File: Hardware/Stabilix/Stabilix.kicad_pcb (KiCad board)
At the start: 2 copper layers, 68.6 x 53.3 mm, 28 parts, among them J1 NEMA17-M1, J2 NEMA17-M2, J3 KF35-2P Battery, J4 Power Switch, J5 Servo, J6 Expansion, U1 AMS1117-5.0, U2 AMS1117-5.0, U3 A4988_STEPPER_MOTOR_DRIVER_CA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, U4 A4988_STEPPER_MOTOR_DRIVER_CA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, U5 module_mpu6050, U6 ESP32-DEVKIT-V1

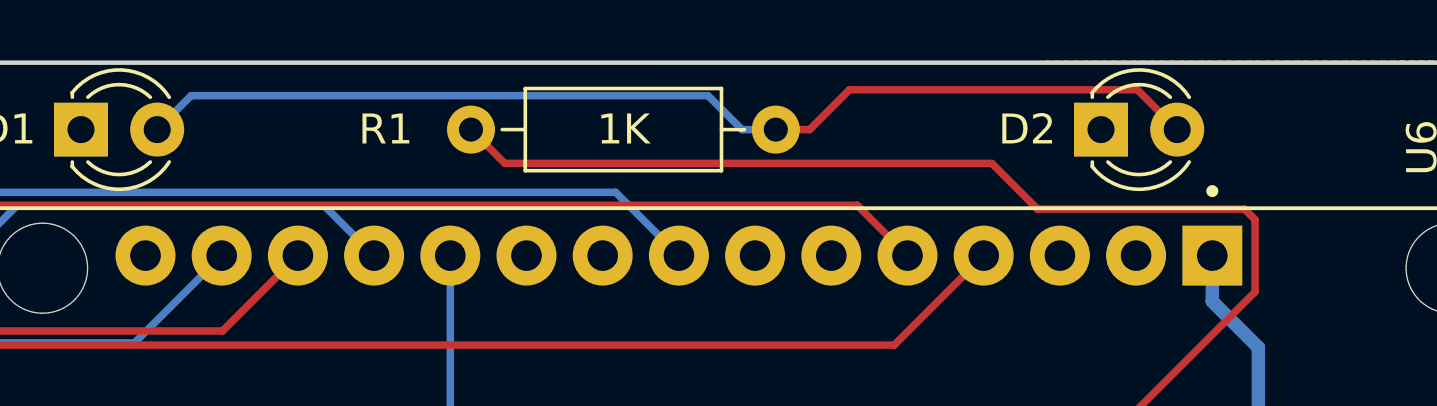
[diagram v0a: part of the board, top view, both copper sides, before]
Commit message: Footprint adjustments
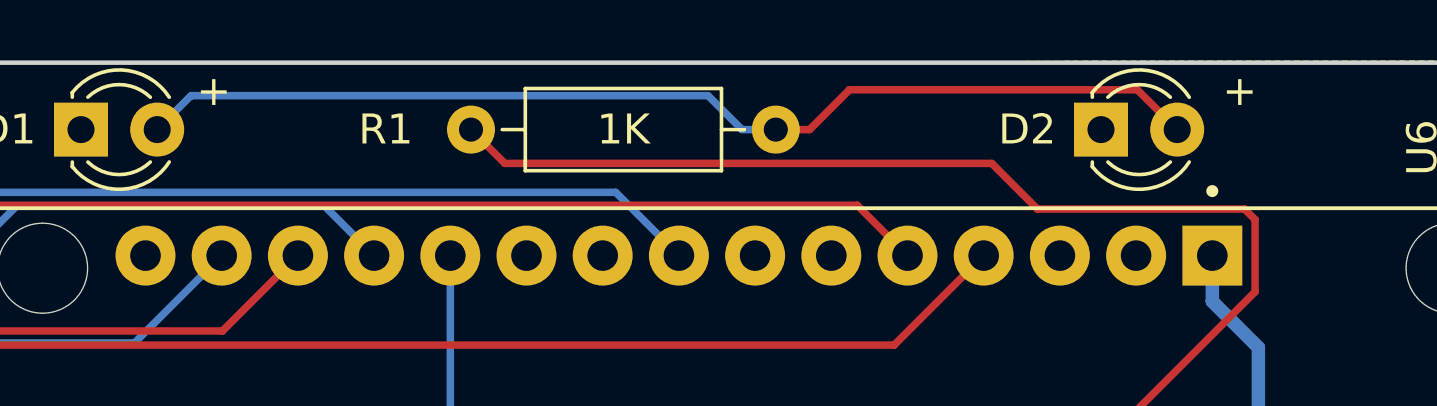
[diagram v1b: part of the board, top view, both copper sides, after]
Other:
- board text added: "+"
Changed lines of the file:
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@@
     (attr board_only exclude_from_pos_files exclude_from_bom)
     (fp_text reference "kibuzzard-6589FCE6" (at 0 -3.891492) (layer "F.SilkS") hide
-        (effects (font (size 0 0)))
+        (effects (font (size 0 0) (thickness 0.15)))
     )
     (fp_text value "G***" (at 0 3.891492) (layer "F.SilkS") hide
-        (effects (font (size 0 0)))
+        (effects (font (size 0 0) (thickness 0.15)))
     )
     (fp_poly
@@
     (pad "2" thru_hole circle (at 5.08 0 270) (size 3 3) (drill 1.52) (layers "*.Cu" "*.Mask")
       (net 42 "Net-(J3-Pin_2)") (pinfunction "Pin_2") (pintype "passive"))
-    (model "${KIPRJMOD}/libraries/TerminalBlock_bornier-2_P5.08mm.wrl"
-      (offset (xyz 2.54 0 0))
+    (model "${KICAD7_3DMODEL_DIR}/TerminalBlock_Phoenix.3dshapes/TerminalBlock_Phoenix_MKDS-1,5-2_1x02_P5.00mm_Horizontal.wrl"
+      (offset (xyz 0 0 0))
       (scale (xyz 1 1 1))
       (rotate (xyz 0 0 0))
@@
     (attr board_only exclude_from_pos_files exclude_from_bom)
     (fp_text reference "kibuzzard-6589FE5A" (at 0 -3.881173) (layer "F.SilkS") hide
-        (effects (font (size 0 0)))
+        (effects (font (size 0 0) (thickness 0.15)))
     )
     (fp_text value "G***" (at 0 3.881173) (layer "F.SilkS") hide
-        (effects (font (size 0 0)))
+        (effects (font (size 0 0) (thickness 0.15)))
     )
     (fp_poly
@@
     (attr board_only exclude_from_pos_files exclude_from_bom)
     (fp_text reference "kibuzzard-6589FE3E" (at 0 -3.87006) (layer "F.SilkS") hide
-        (effects (font (size 0 0)))
+        (effects (font (size 0 0) (thickness 0.15)))
     )
     (fp_text value "G***" (at 0 3.87006) (layer "F.SilkS") hide
-        (effects (font (size 0 0)))
+        (effects (font (size 0 0) (thickness 0.15)))
     )
     (fp_poly
@@
     (effects (font (size 0.8 0.8) (thickness 0.15)) (justify left bottom))
   )
+  (gr_text "+" (at 125 70.8) (layer "F.SilkS")
+    (effects (font (size 1 1) (thickness 0.15)) (justify left bottom mirror))
+  )
   (gr_text "D4" (at 109.1 78.2) (layer "F.SilkS")
     (effects (font (size 0.8 0.8) (thickness 0.15)) (justify left bottom))
   )
+  (gr_text "+" (at 159.2 70.8) (layer "F.SilkS")
+    (effects (font (size 1 1) (thickness 0.15)) (justify left bottom mirror))
+  )
   (gr_text "3V3" (at 103.8 78.2) (layer "F.SilkS")

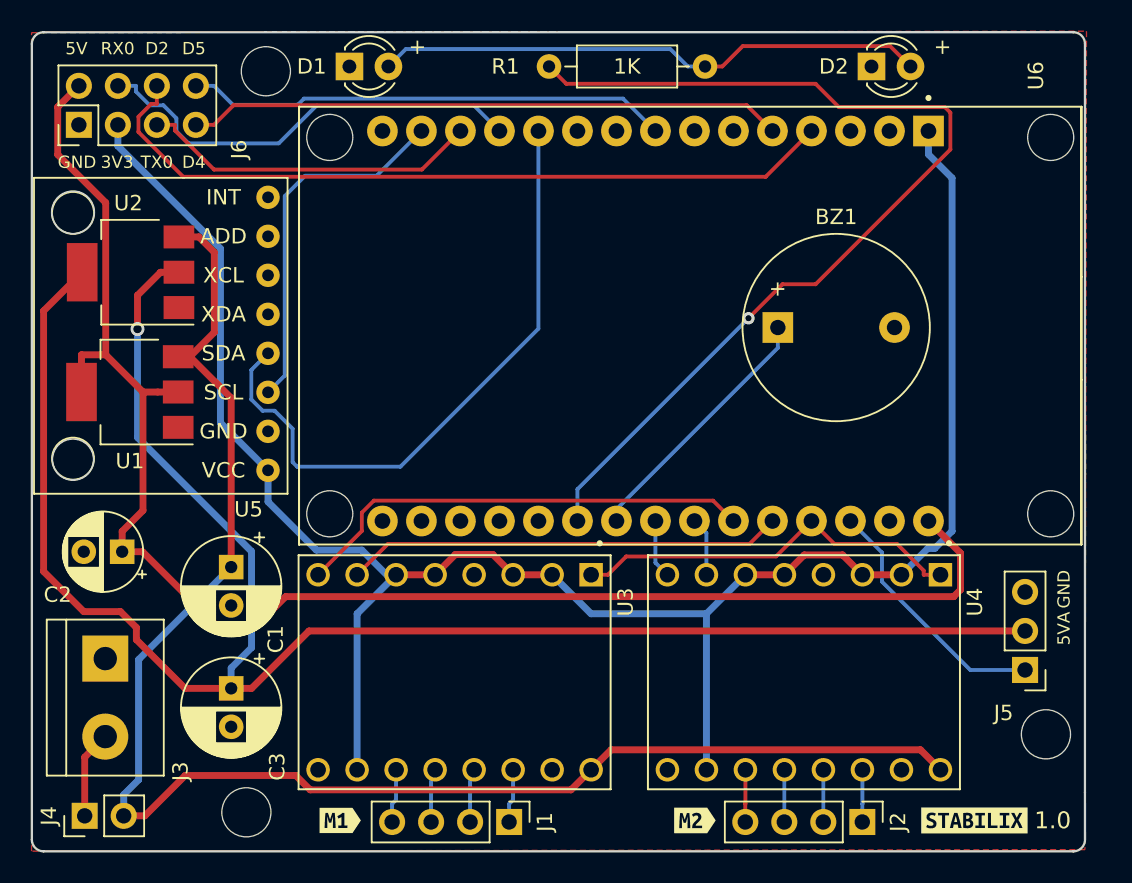
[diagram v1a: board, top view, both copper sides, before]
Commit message: fixes on the screw holes
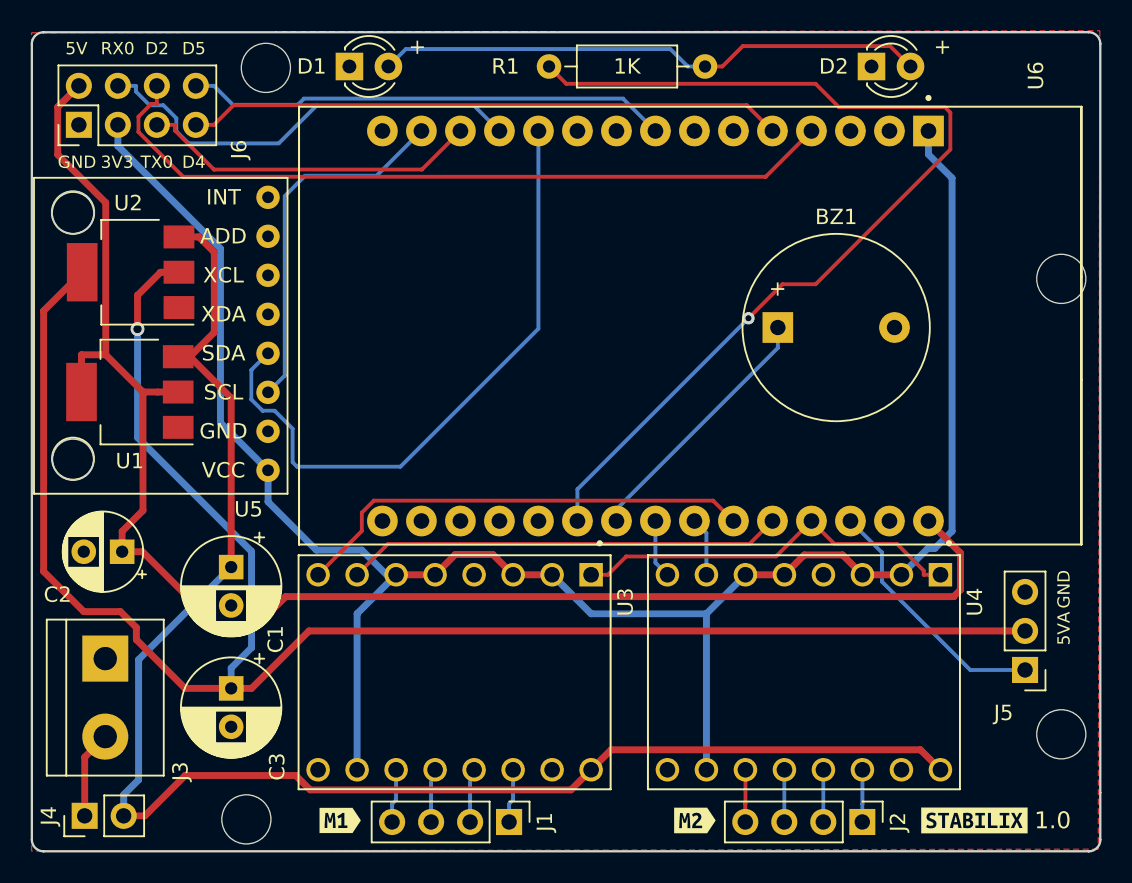
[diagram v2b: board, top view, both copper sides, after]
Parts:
- added MH4: MountingHole_3.2mm, Arduino_MountingHole:MountingHole_3.2mm, F.Cu at (166.4, 85.3)
- moved MH4 1.00 mm to (166.4, 115.0)
- moved MH2 0.23 mm to (113.3, 120.3)
- moved MH1 0.11 mm to (114.6, 71.7)
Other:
- board size 68.6 x 53.3 mm -> 69.6 x 53.3 mm
- board text added: "Stabilix Self-Balancing Robot Based on JJRobots open source B-Robot EVO project"
- board text added: "crisag@2023"
- board text removed: "Stabilix Self-Balancing Robot Based on JJRobots open source B-Robot EVO project crisag@2023"
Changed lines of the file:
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@@
   )
   (footprint "Arduino_MountingHole:MountingHole_3.2mm" (layer "F.Cu")
-    (at 113.29 120.07)
+    (at 113.29 120.3)
     (descr "Mounting Hole 3.2mm, no annular, M3")
     (tags "mounting hole 3.2mm no annular m3")
@@
     (fp_circle (center 0 0) (end 1.7 0)
       (stroke (width 0.05) (type solid)) (fill none) (layer "F.CrtYd"))
-    (pad "" np_thru_hole circle (at 0 0) (size 3.2 3.2) (drill 3.2) (layers "F&B.Cu" "*.Mask"))
+    (pad "" np_thru_hole circle (at 0 0.23) (size 3.2 3.2) (drill 3.2) (layers "F&B.Cu" "*.Mask"))
   )
   (footprint "Resistor_THT:R_Axial_DIN0207_L6.3mm_D2.5mm_P10.16mm_Horizontal" (layer "F.Cu")
@@
       (stroke (width 0) (type solid)) (fill solid) (layer "F.SilkS"))
   )
+  (footprint "Arduino_MountingHole:MountingHole_3.2mm" (layer "F.Cu")
+    (at 166.36 85.33)
+    (descr "Mounting Hole 3.2mm, no annular, M3")
+    (tags "mounting hole 3.2mm no annular m3")
+    (attr board_only exclude_from_pos_files exclude_from_bom)
+    (fp_text reference "MH4" (at 0 -4.2) (layer "F.SilkS") hide
+        (effects (font (size 1 1) (thickness 0.15)))
+    )
+    (fp_text value "MountingHole_3.2mm" (at 0 4.2) (layer "F.Fab") hide
+        (effects (font (size 1 1) (thickness 0.15)))
+    )
+    (fp_text user "${REFERENCE}" (at 0.3 0) (layer "F.Fab") hide
+        (effects (font (size 1 1) (thickness 0.15)))
+    )
+    (fp_circle (center 0 0) (end 1.7 0)
+      (stroke (width 0.05) (type solid)) (fill none) (layer "F.CrtYd"))
+    (pad "" np_thru_hole circle (at 0 0) (size 3.2 3.2) (drill 3.2) (layers "F&B.Cu" "*.Mask"))
+  )
   (footprint "Capacitor_THT:CP_Radial_D5.0mm_P2.50mm" (layer "F.Cu")
     (at 105.2 103.1 180)
@@
   )
   (footprint "Arduino_MountingHole:MountingHole_3.2mm" (layer "F.Cu")
-    (at 165.36 114.99)
+    (at 166.36 114.99)
     (descr "Mounting Hole 3.2mm, no annular, M3")
     (tags "mounting hole 3.2mm no annular m3")
@@
     (fp_circle (center -14.85 -15.515) (end -14.75 -15.515)
       (stroke (width 0.2) (type solid)) (fill none) (layer "F.Fab"))
-    (pad "" np_thru_hole circle (at -12.28 -23.475 270) (size 3 3) (drill 3) (layers "*.Cu" "*.Mask"))
-    (pad "" np_thru_hole circle (at -12.28 23.475 270) (size 3 3) (drill 3) (layers "*.Cu" "*.Mask"))
-    (pad "" np_thru_hole circle (at 12.23 -23.475 270) (size 3 3) (drill 3) (layers "*.Cu" "*.Mask"))
-    (pad "" np_thru_hole circle (at 12.23 23.475 270) (size 3 3) (drill 3) (layers "*.Cu" "*.Mask"))
     (pad "1" thru_hole rect (at -12.7 -15.515 270) (size 2 2) (drill 1.02) (layers "*.Cu" "*.Mask")
       (net 20 "+3.3V") (pinfunction "3V3") (pintype "output") (solder_mask_margin 0.102))
@@
   )
   (footprint "Arduino_MountingHole:MountingHole_3.2mm" (layer "F.Cu")
-    (at 114.56 71.81)
+    (at 114.56 71.7)
     (descr "Mounting Hole 3.2mm, no annular, M3")
     (tags "mounting hole 3.2mm no annular m3")
@@
     (fp_circle (center 0 0) (end 1.7 0)
       (stroke (width 0.05) (type solid)) (fill none) (layer "F.CrtYd"))
-    (pad "" np_thru_hole circle (at 0 0) (size 3.2 3.2) (drill 3.2) (layers "F&B.Cu" "*.Mask"))
+    (pad "" np_thru_hole circle (at 0 -0.11) (size 3.2 3.2) (drill 3.2) (layers "F&B.Cu" "*.Mask"))
   )
   (footprint "kibuzzard-6589FE5A" (layer "F.Cu")
@@
       (stroke (width 0.01) (type solid)) (fill solid) (layer "B.SilkS"))
   )
-  (gr_line (start 167.9 118.8) (end 167.903185 121.851185)
+  (gr_line (start 168.9 118.8) (end 168.9 121.851185)
     (stroke (width 0.15) (type default)) (layer "Edge.Cuts"))
   (gr_arc (start 99.32 70.032) (mid 99.543185 69.493185) (end 100.082 69.27)
     (stroke (width 0.15) (type solid)) (layer "Edge.Cuts"))
-  (gr_line (start 100.082 69.27) (end 167.141185 69.268)
+  (gr_line (start 100.082 69.27) (end 168.141185 69.268)
     (stroke (width 0.15) (type solid)) (layer "Edge.Cuts"))
   (gr_line (start 99.32 121.848) (end 99.32 70.032)
@@
   (gr_circle (center 102 81) (end 101.3 79.8)
     (stroke (width 0.1) (type default)) (fill none) (layer "Edge.Cuts"))
-  (gr_arc (start 167.903185 121.851185) (mid 167.68 122.39) (end 167.141185 122.613185)
+  (gr_arc (start 168.903185 121.851185) (mid 168.680005 122.390005) (end 168.141185 122.613185)
     (stroke (width 0.15) (type solid)) (layer "Edge.Cuts"))
   (gr_arc (start 100.082 122.61) (mid 99.543185 122.386815) (end 99.32 121.848)
     (stroke (width 0.15) (type solid)) (layer "Edge.Cuts"))
-  (gr_line (start 167.138 122.61) (end 100.082 122.61)
+  (gr_line (start 168.138 122.61) (end 100.082 122.61)
     (stroke (width 0.15) (type solid)) (layer "Edge.Cuts"))
   (gr_circle (center 102 97.1) (end 101.4 95.9)
     (stroke (width 0.1) (type default)) (fill none) (layer "Edge.Cuts"))
-  (gr_line (start 167.903185 70.03) (end 167.9 118.8)
+  (gr_line (start 168.9 70.03) (end 168.9 118.8)
     (stroke (width 0.15) (type solid)) (layer "Edge.Cuts"))
-  (gr_arc (start 167.141185 69.268) (mid 167.68 69.491185) (end 167.903185 70.03)
+  (gr_arc (start 168.141185 69.268) (mid 168.68001 69.491179) (end 168.903185 70.03)
     (stroke (width 0.15) (type solid)) (layer "Edge.Cuts"))
-  (gr_text "Stabilix Self-Balancing Robot\nBased on JJRobots open source \nB-Robot EVO project\ncrisag@2023" (at 166.4 88.5 90) (layer "B.SilkS")
+  (gr_text "Stabilix Self-Balancing Robot\nBased on JJRobots open source \nB-Robot EVO project" (at 164.01 88.58 90) (layer "B.SilkS")
     (effects (font (size 1 1) (thickness 0.15)) (justify bottom mirror))
   )
+  (gr_text "crisag@2023" (at 167.89 71.01 90) (layer "B.SilkS")
+    (effects (font (size 1 1) (thickness 0.15)) (justify left bottom mirror))
+  )
   (gr_text "5VA" (at 167 109.2 90) (layer "F.SilkS")
     (effects (font (size 0.8 0.8) (thickness 0.15)) (justify left bottom))
@@
       (pts
         (xy 99.3 69.3)
-        (xy 168 69.2)
-        (xy 167.9 122.5)
+        (xy 168.87 69.17)
+        (xy 168.77 122.47)
         (xy 99.3 122.6)
       )
